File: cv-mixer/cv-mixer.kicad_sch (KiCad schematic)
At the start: 42 parts, among them J1 Input A1, J10 Pot, J11 Input B3, J12 Pot, J13 Pot, J14 Output A, J15 Pot, J16 Output B, J17 Power, J18 Power, J19 Power, J2 Pot, J3 Input A2, J4 Pot, J5 Input A3, J6 Pot, J7 Input B1, J8 Pot, J9 Input B2, U1 TL074

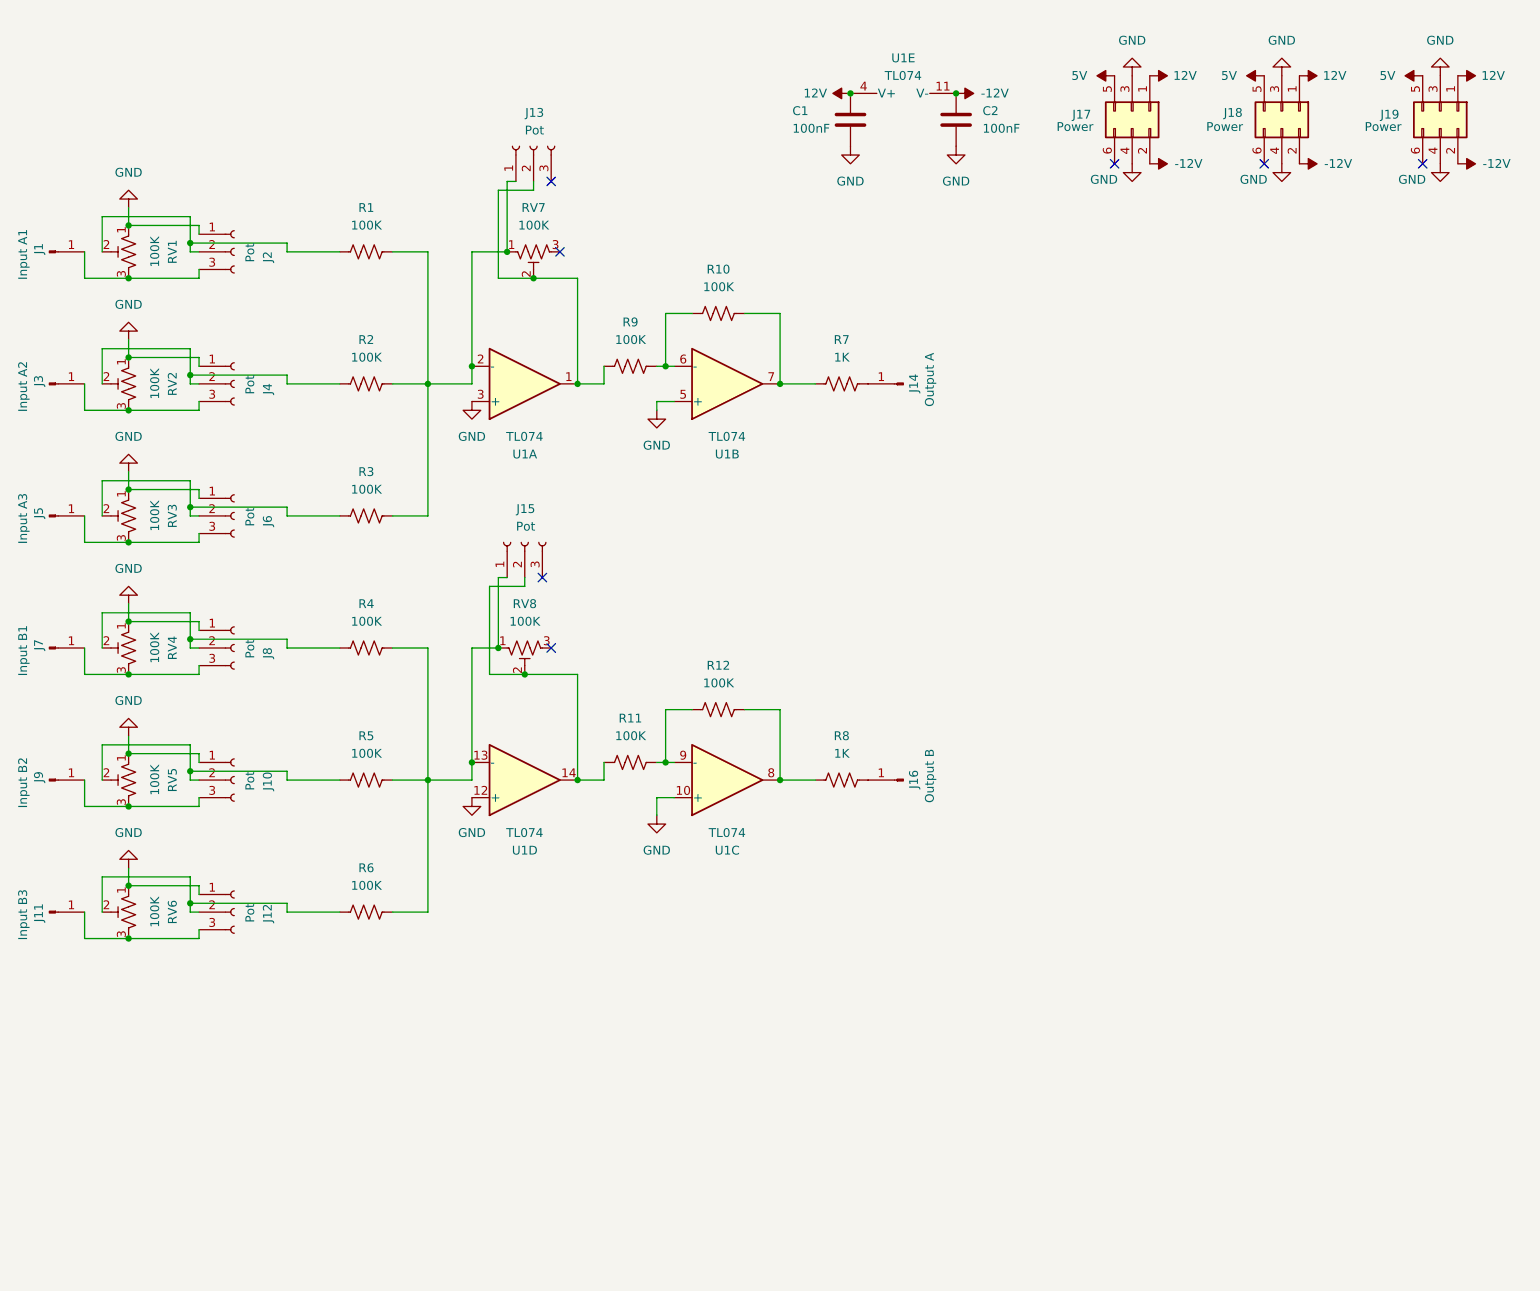
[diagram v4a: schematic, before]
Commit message: Multilayer cv-mixer
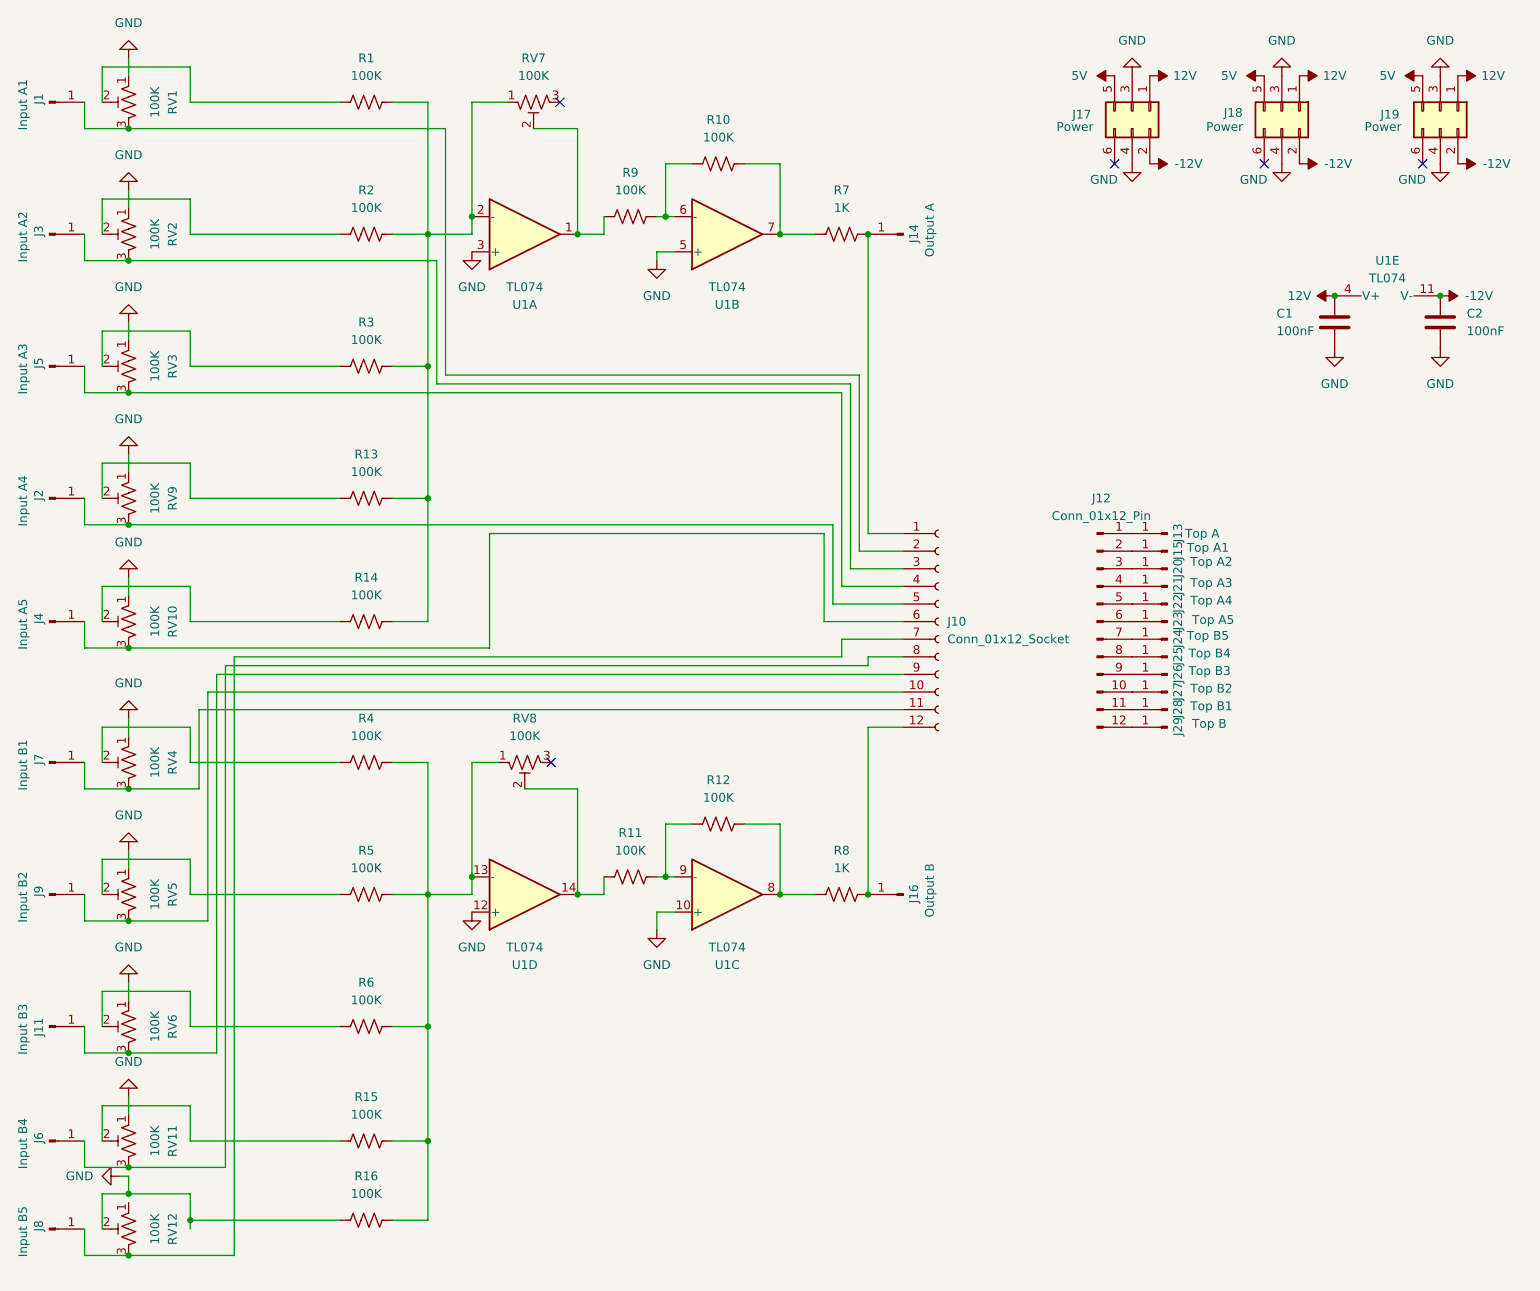
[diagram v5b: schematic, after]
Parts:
- removed J10, J12, J13, J15, J2, J4, J6, J8: Pot, modular2:pot, symbol Connector:Conn_01x03_Socket
- added J10: Conn_01x12_Socket, Connector_PinSocket_2.54mm:PinSocket_1x12_P2.54mm_Vertical, symbol Connector:Conn_01x12_Socket
- added J12: Conn_01x12_Pin, Connector_PinHeader_2.54mm:PinHeader_1x12_P2.54mm_Vertical, symbol Connector:Conn_01x12_Pin
- added J13: Top A, modular2:banana-jack, symbol Connector:Conn_01x01_Pin
- added J15: Top A1, modular2:banana-jack, symbol Connector:Conn_01x01_Pin
- added J2: Input A4, modular2:banana-jack, symbol Connector:Conn_01x01_Pin
- added J20: Top A2, modular2:banana-jack, symbol Connector:Conn_01x01_Pin
- added J21: Top A3, modular2:banana-jack, symbol Connector:Conn_01x01_Pin
- added J22: Top A4, modular2:banana-jack, symbol Connector:Conn_01x01_Pin
- added J23: Top A5, modular2:banana-jack, symbol Connector:Conn_01x01_Pin
- added J24: Top B5, modular2:banana-jack, symbol Connector:Conn_01x01_Pin
- added J25: Top B4, modular2:banana-jack, symbol Connector:Conn_01x01_Pin
- added J26: Top B3, modular2:banana-jack, symbol Connector:Conn_01x01_Pin
- added J27: Top B2, modular2:banana-jack, symbol Connector:Conn_01x01_Pin
- added J28: Top B1, modular2:banana-jack, symbol Connector:Conn_01x01_Pin
- added J29: Top B, modular2:banana-jack, symbol Connector:Conn_01x01_Pin
- added J4: Input A5, modular2:banana-jack, symbol Connector:Conn_01x01_Pin
- added J6: Input B4, modular2:banana-jack, symbol Connector:Conn_01x01_Pin
- added J8: Input B5, modular2:banana-jack, symbol Connector:Conn_01x01_Pin
- added R13, R14, R15, R16: 100K, Resistor_THT:R_Axial_DIN0207_L6.3mm_D2.5mm_P10.16mm_Horizontal, symbol Device:R_US
- added RV10, RV11, RV12, RV9: 100K, modular2:Potentiometer_Alps_RK09K_Single_Vertical - knob padding, symbol Device:R_Potentiometer_Trim_US
- RV1, RV2, RV3, RV4, RV5, RV6, RV7, RV8: footprint modular2:pot-socket -> modular2:Potentiometer_Alps_RK09K_Single_Vertical - knob padding
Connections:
- net GND: now also R16.1, RV10.1, RV11.1, RV12.2, RV9.1
- net at J1.1 (Pin_1), RV1.3: now also J10.2 (Pin_2)
- net at R1.2, R2.2, R3.2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: now also R13.2, R14.2
- net at J3.1 (Pin_1), RV2.3: now also J10.3 (Pin_3)
- net at J5.1 (Pin_1), RV3.3: now also J10.4 (Pin_4)
- net at J7.1 (Pin_1), RV4.3: now also J10.11 (Pin_11)
- net at J9.1 (Pin_1), RV5.3: now also J10.10 (Pin_10)
- net at J11.1 (Pin_1), RV6.3: now also J10.9 (Pin_9)
- net at R4.2, R5.2, R6.2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: now also R15.2, R16.2
- net at J14.1 (Pin_1), R7.2: now also J10.1 (Pin_1)
- net at J16.1 (Pin_1), R8.2: now also J10.12 (Pin_12)
- new net: J12.4 (Pin_4), J21.1 (Pin_1)
- new net: J12.2 (Pin_2), J15.1 (Pin_1)
- new net: J10.5 (Pin_5), J2.1 (Pin_1), RV9.3
- new net: J10.6 (Pin_6), J4.1 (Pin_1), RV10.3
- new net: J10.7 (Pin_7), J8.1 (Pin_1), RV12.3
- new net: J10.8 (Pin_8), J6.1 (Pin_1), RV11.3
- new net: R14.1, RV10.2
- new net: J12.10 (Pin_10), J27.1 (Pin_1)
- new net: J12.1 (Pin_1), J13.1 (Pin_1)
- new net: J12.11 (Pin_11), J28.1 (Pin_1)
- new net: J12.12 (Pin_12), J29.1 (Pin_1)
- new net: J12.3 (Pin_3), J20.1 (Pin_1)
- new net: J12.5 (Pin_5), J22.1 (Pin_1)
- new net: J12.6 (Pin_6), J23.1 (Pin_1)
- new net: J12.7 (Pin_7), J24.1 (Pin_1)
- new net: J12.8 (Pin_8), J25.1 (Pin_1)
- new net: J12.9 (Pin_9), J26.1 (Pin_1)
- new net: R13.1, RV9.2
- new net: R15.1, RV11.2
- no-connect marks 7 -> 5
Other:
- moved on the sheet: C1, C2, J1, J11, J14, J16, J3, J5, J7, J9, R1, R10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
